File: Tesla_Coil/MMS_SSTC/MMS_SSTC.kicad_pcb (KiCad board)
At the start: 2 copper layers, 85 x 85.5 mm, 41 parts, among them J1 Screw_Terminal_01x02, J2 Screw_Terminal_01x02, Q1 FQA8N100C, U1 NE555P, U2 UCC37322P, U3 CD74HC14E, U4 LM7812_TO220, U5 LM7805_TO220

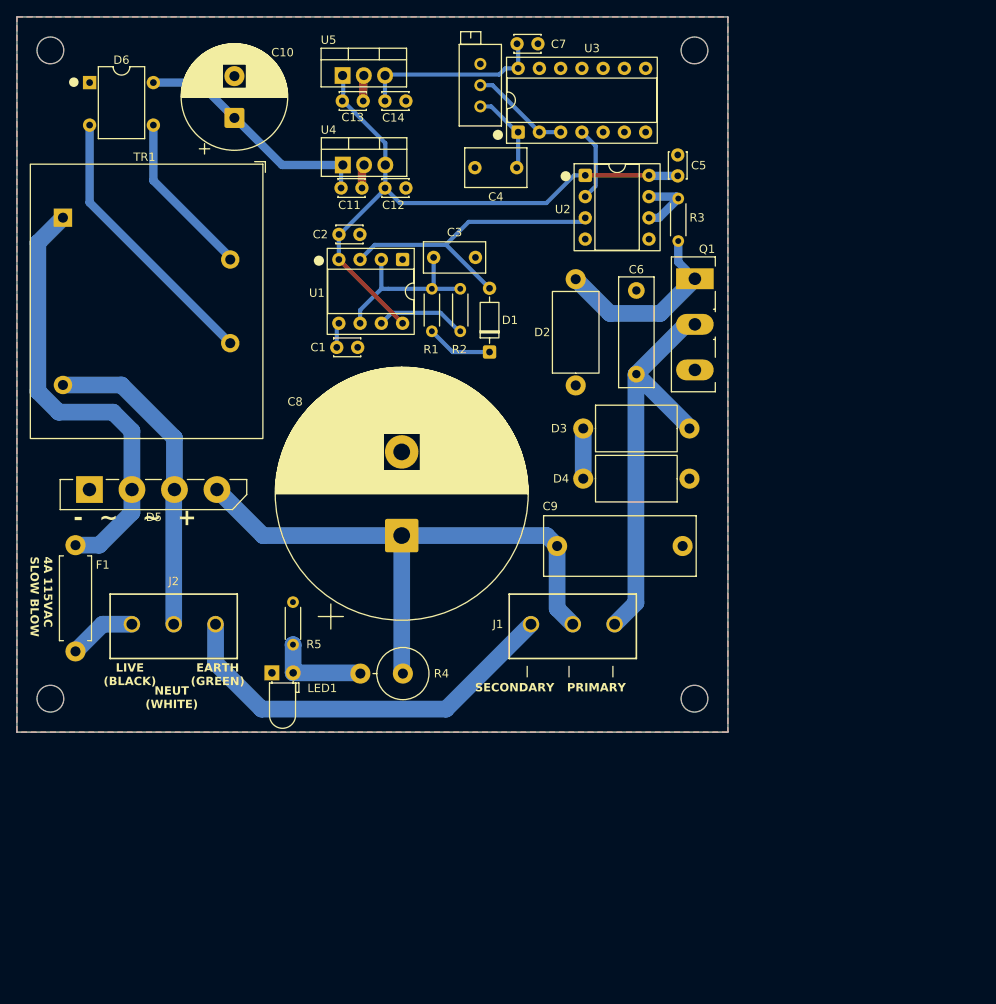
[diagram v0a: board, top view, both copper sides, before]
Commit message: SSTC PCB finished
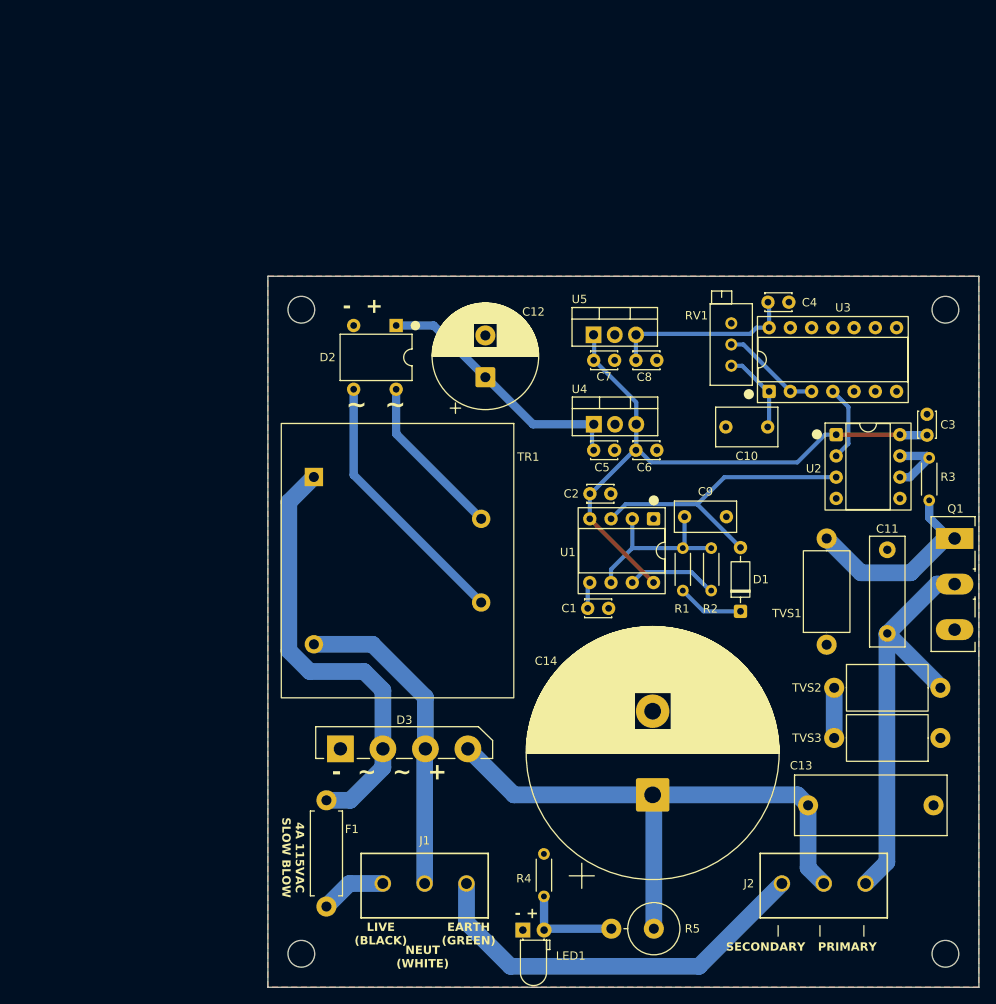
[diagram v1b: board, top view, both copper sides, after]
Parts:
- D3: renamed from D5; footprint Diode_THT:Diode_Bridge_Vishay_GBU -> Diode_THT:Diode_Bridge_Vishay_GBL
- R2: value 150k -> 68k
- RV1: value 2.2k -> 5k
- moved D2 46.8 mm to (105.3, 65.9), turned to -90 degrees
- moved Q1 43.9 mm to (172.1, 91.3)
- moved C5 43.5 mm to (128.9, 80.8)
- moved C6 43.4 mm to (134.0, 80.8)
- moved C1 43.3 mm to (128.2, 99.7)
- moved C7 43.2 mm to (128.9, 70.0)
- moved C13 43.1 mm to (154.6, 123.2)
- moved TVS1 43.1 mm to (156.8, 104.0)
- moved U4 43.1 mm to (129.0, 77.7)
- moved R3 43.1 mm to (169.1, 86.8)
- moved C11 43.1 mm to (164.1, 102.7)
- moved C12 43.1 mm to (116.0, 72.1)
- moved C14 43.1 mm to (136.0, 122.0)
- moved C2 43.1 mm to (128.5, 86.0)
- moved C8 43.1 mm to (134.0, 70.0)
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- renumbered C4 to C10, C6 to C11, C10 to C12, C9 to C13, C8 to C14, C5 to C3, C7 to C4, C11 to C5, C12 to C6, C13 to C7, C14 to C8, C3 to C9, D6 to D2, J2 to J1, J1 to J2, R5 to R4, R4 to R5, D2 to TVS1, D3 to TVS2, D4 to TVS3
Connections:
- C12 pad 1: Net-(D6-+) -> Net-(D2-+)
- C5 pad 1: Net-(D6-+) -> Net-(D2-+)
- D2 pad 1: GND -> Net-(D2-+)
- D2 pad 2: Net-(D6-Pad2) -> GND
- D2 pad 3: Net-(D6-Pad3) -> Net-(D2-Pad3)
- D2 pad 4: Net-(D6-+) -> Net-(D2-Pad4)
- TR1 pad 3: Net-(D6-Pad3) -> Net-(D2-Pad4)
- TR1 pad 4: Net-(D6-Pad2) -> Net-(D2-Pad3)
- U4 pad 1: Net-(D6-+) -> Net-(D2-+)
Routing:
- net Net-(D6-Pad2): track 33.0 -> 0.00 mm
- net Net-(D2-Pad3): track 0.00 -> 31.8 mm
- net Net-(D2-+): track 0.00 -> 31.4 mm
- net Net-(D6-+): track 29.6 -> 0.00 mm
- net Net-(D2-Pad4): track 0.00 -> 20.0 mm
- net Net-(D6-Pad3): track 19.9 -> 0.00 mm
- net GND: track 9.00 -> 0.16 mm
- net /GATE: track 23.0 -> 24.8 mm
- net /DRAIN: track 49.6 -> 50.6 mm
- net Net-(LED1-A): track 11.5 -> 12.1 mm
- net +170V: track 70.1 -> 69.6 mm
- net AC_PROT: track 53.3 -> 52.8 mm
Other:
- board size 85 x 85.5 mm -> 85 x 85 mm
- board text added: "- +"
- board text added: "MMS SSTC {dblquote}Lambda{dblquote} Mk. 1 Design by William Layne"
- board text added: "~ ~"
